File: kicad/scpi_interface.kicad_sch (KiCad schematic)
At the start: 17 parts, among them J5 N2510-6002-RB, U17 AM1SS-1203SJZ, U22 ADuM121N, U23 MAX3221ExPWR

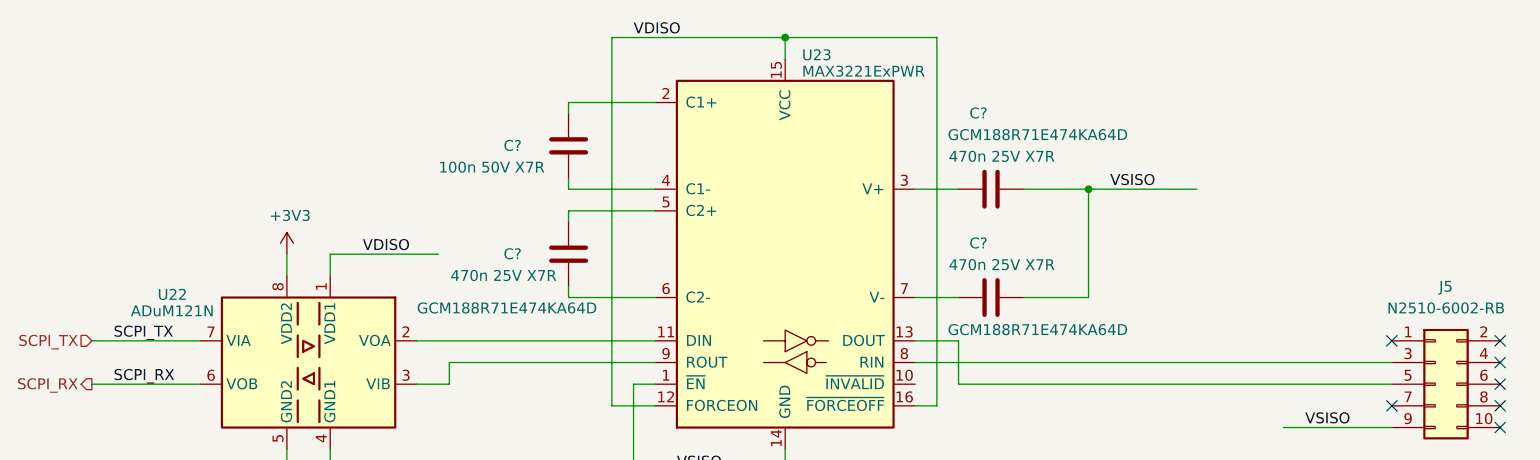
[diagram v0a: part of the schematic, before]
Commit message: bugfix: driver for 4th T, capacitors for input amps
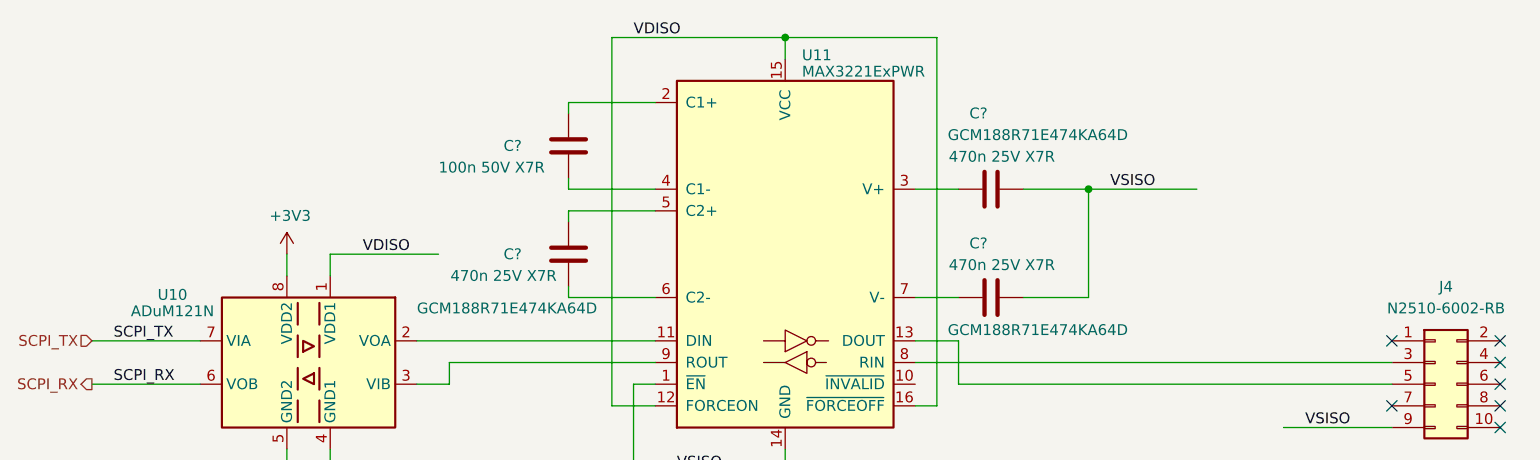
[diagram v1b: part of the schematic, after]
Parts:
- renumbered J5 to J4, U22 to U10, U23 to U11
